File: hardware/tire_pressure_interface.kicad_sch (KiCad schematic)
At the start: 1 part, among them U3 XIAO-ESP32-S3-DIP

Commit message: reorganization of project folders acording to templates
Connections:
- net +3.3V renamed +3V3
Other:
- sheet Micro_SD_Card ports: added DET; removed none
- sheet STM32 ports: added DET; removed none
- company: (none) -> Author:

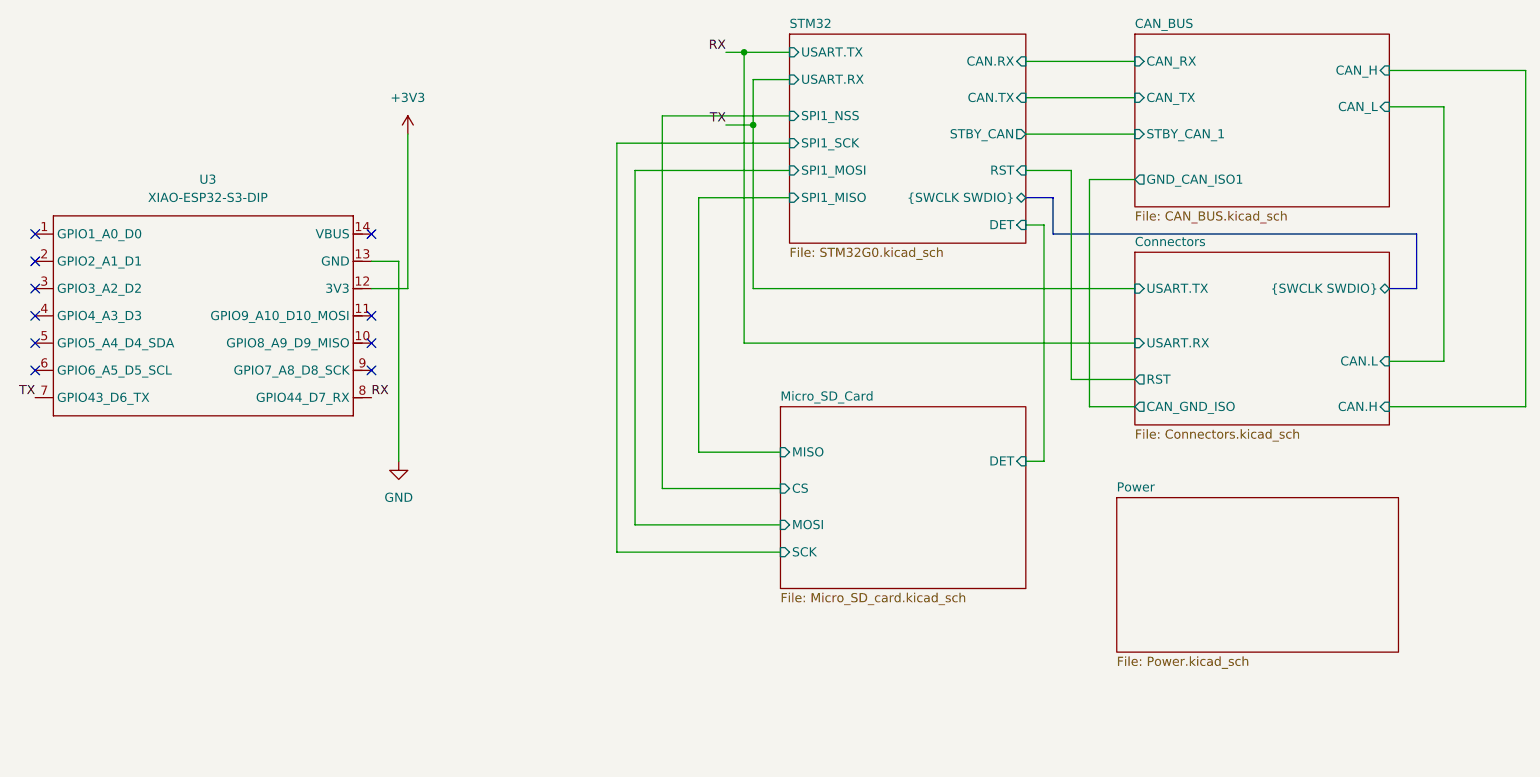
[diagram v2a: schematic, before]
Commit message: reorganize SPI signals into bus
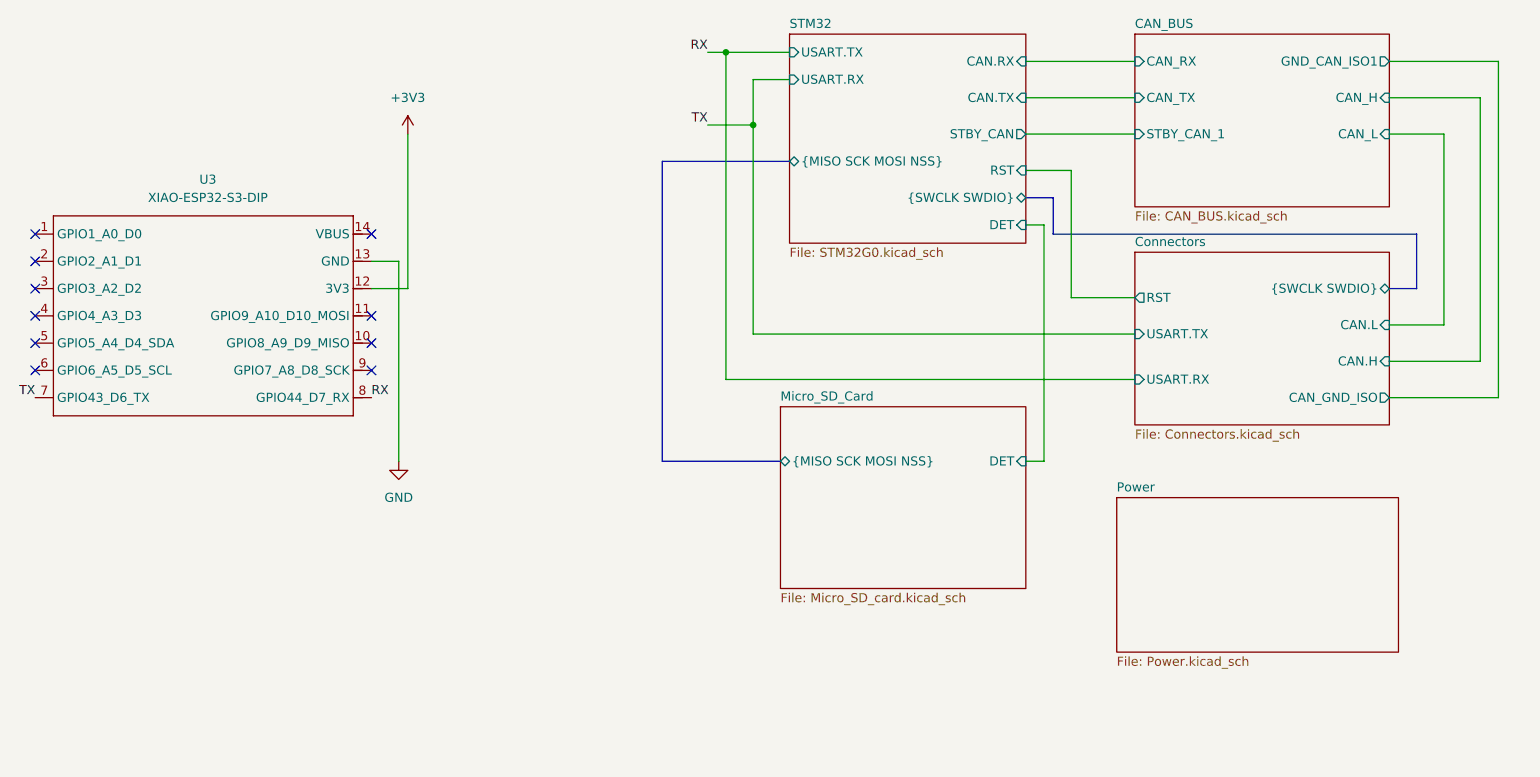
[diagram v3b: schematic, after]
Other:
- sheet Micro_SD_Card ports: added {MISO SCK MOSI NSS}; removed CS, MISO, MOSI, SCK
- sheet STM32 ports: added {MISO SCK MOSI NSS}; removed SPI1_MISO, SPI1_MOSI, SPI1_NSS, SPI1_SCK

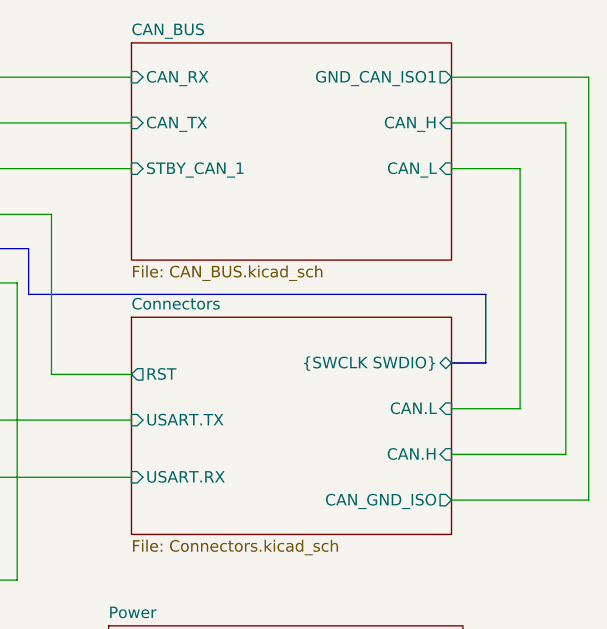
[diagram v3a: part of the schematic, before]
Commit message: changed layout
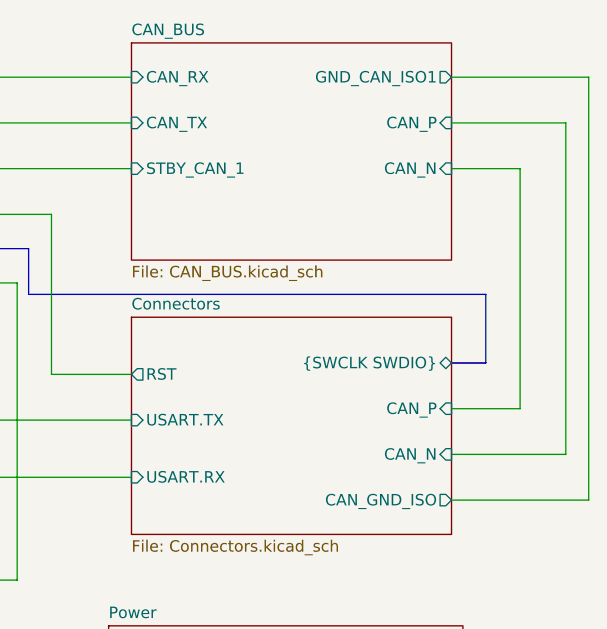
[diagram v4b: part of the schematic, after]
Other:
- sheet CAN_BUS ports: added CAN_N, CAN_P; removed CAN_H, CAN_L
- sheet Connectors ports: added CAN_N, CAN_P; removed CAN.H, CAN.L
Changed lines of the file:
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@@
 			)
 		)
-		(pin "CAN.H" input
+		(pin "CAN_N" input
 			(at 233.68 90.17 0)
 			(effects
@@
 			)
 		)
-		(pin "CAN.L" input
+		(pin "CAN_P" input
 			(at 233.68 85.09 0)
 			(effects
@@
 			)
 		)
-		(pin "CAN_H" input
+		(pin "CAN_P" input
 			(at 233.68 53.34 0)
 			(effects
@@
 			)
 		)
-		(pin "CAN_L" input
+		(pin "CAN_N" input
 			(at 233.68 58.42 0)
 			(effects
